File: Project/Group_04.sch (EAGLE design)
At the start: 29 parts, among them J1 POWER_JACKPTH_LOCK, U1 +12v

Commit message: modified frame and fixed component
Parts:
- U$1: device mylibrary_1:TMUX1208 -> Group_04_Library:TMUX1208
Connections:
- new net N$2: U$1.EN
- net 5V: no longer U$1.EN
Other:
- note added: "4-Channel I2C"
- note added: "Analog Temperature Sensor"
- note added: "I2C Connectors"
- note added: "Light sensor"
- note added: "Power"
- note added: "The I2C expander is used to connect several BME280 sensors outside the PCB through these connectors"
- moved on the sheet: C1, C2, C3, D1, J1, J2, J3, J4, J5, J6, J7, J8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

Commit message: fixed error on 5V pin
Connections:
- removed net N$2: U$1.EN
- net 5V: now also U$1.EN
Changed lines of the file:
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@@
 <part name="GND5" library="SparkFun-PowerSymbols" deviceset="GND" device=""/>
 <part name="J4" library="SparkFun-Connectors" deviceset="CONN_08" device="LOCK"/>
-<part name="SUPPLY8" library="SparkFun-PowerSymbols" deviceset="5V" device=""/>
 <part name="GND6" library="SparkFun-PowerSymbols" deviceset="GND" device=""/>
 <part name="C3" library="SparkFun-Capacitors" deviceset="0.1UF" device="-KIT-EZ-50V-20%" value="0.1uF"/>
@@
 <part name="U$1" library="Group_04_Library" deviceset="TMUX1208" device=""/>
 <part name="FRAME2" library="frames" library_urn="urn:adsk.eagle:library:229" deviceset="A4L-LOC" device=""/>
+<part name="SUPPLY8" library="SparkFun-PowerSymbols" deviceset="5V" device=""/>
 </parts>
 <sheets>
@@
 <attribute name="NAME" x="370.84" y="112.268" size="1.778" layer="95" font="vector"/>
 </instance>
-<instance part="SUPPLY8" gate="G$1" x="429.26" y="88.9" smashed="yes" rot="R270">
-<attribute name="VALUE" x="432.054" y="88.9" size="1.778" layer="96" rot="R270" align="bottom-center"/>
-</instance>
 <instance part="GND6" gate="1" x="424.18" y="78.74" smashed="yes">
 <attribute name="VALUE" x="424.18" y="78.486" size="1.778" layer="96" align="top-center"/>
@@
 <attribute name="LAST_DATE_TIME" x="494.03" y="20.32" size="2.286" layer="94"/>
 <attribute name="SHEET" x="507.365" y="15.24" size="2.54" layer="94"/>
+</instance>
+<instance part="SUPPLY8" gate="G$1" x="449.58" y="88.9" smashed="yes">
+<attribute name="VALUE" x="449.58" y="91.694" size="1.778" layer="96" align="bottom-center"/>
 </instance>
 </instances>
@@
 <junction x="429.26" y="119.38"/>
 </segment>
+<segment>
+<pinref part="U$1" gate="G$1" pin="EN"/>
+<pinref part="SUPPLY8" gate="G$1" pin="5V"/>
+<wire x1="421.64" y1="88.9" x2="449.58" y2="88.9" width="0.1524" layer="91"/>
+</segment>
 </net>
 <net name="MUX_OUT/1.4C" class="0">
@@
 </segment>
 </net>
-<net name="N$2" class="0">
-<segment>
-<pinref part="SUPPLY8" gate="G$1" pin="5V"/>
-<wire x1="421.64" y1="88.9" x2="429.26" y2="88.9" width="0.1524" layer="91"/>
-<pinref part="U$1" gate="G$1" pin="EN"/>
-</segment>
-</net>

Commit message: fixed mux connections
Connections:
- removed net MUX_A0/1.3C: U$1.A0
- removed net MUX_A0/2.3C: U$3.P_1.7
- removed net MUX_A1/1.4C: U$1.A1
- removed net MUX_A1/2.3C: U$3.P_1.6
- removed net MUX_A2/1.4C: U$1.A2
- removed net MUX_A2/2.3C: U$3.P_1.5
- removed net MUX_OUT/1.4C: U$1.D
- removed net MUX_OUT/2.5C: U$3.P_1.4
- new net MUX_A0: U$1.A0, U$3.P_1.7
- new net MUX_A1: U$1.A1, U$3.P_1.6
- new net MUX_A2: U$1.A2, U$3.P_1.5
- new net MUX_OUT: U$1.D, U$3.P_1.4
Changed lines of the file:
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@@
-</segment>
-</net>
-<net name="MUX_OUT/1.4C" class="0">
-<segment>
-<wire x1="421.64" y1="93.98" x2="424.18" y2="93.98" width="0.1524" layer="91"/>
-<label x="424.18" y="93.98" size="1.778" layer="95" xref="yes"/>
-<pinref part="U$1" gate="G$1" pin="D"/>
 </segment>
 </net>
@@
 </segment>
 </net>
-<net name="MUX_A0/1.3C" class="0">
+<net name="MUX_OUT" class="0">
 <segment>
-<wire x1="421.64" y1="109.22" x2="424.18" y2="109.22" width="0.1524" layer="91"/>
-<label x="424.18" y="109.22" size="1.778" layer="95" xref="yes"/>
-<pinref part="U$1" gate="G$1" pin="A0"/>
+<pinref part="U$3" gate="G$1" pin="P_1.4"/>
+<wire x1="127" y1="99.06" x2="127" y2="101.6" width="0.1524" layer="91"/>
+<label x="127" y="101.6" size="1.778" layer="95" rot="R90" xref="yes"/>
+</segment>
+<segment>
+<wire x1="421.64" y1="93.98" x2="424.18" y2="93.98" width="0.1524" layer="91"/>
+<label x="424.18" y="93.98" size="1.778" layer="95" xref="yes"/>
+<pinref part="U$1" gate="G$1" pin="D"/>
 </segment>
 </net>
-<net name="MUX_A1/1.4C" class="0">
+<net name="MUX_A2" class="0">
+<segment>
+<pinref part="U$3" gate="G$1" pin="P_1.5"/>
+<wire x1="124.46" y1="99.06" x2="124.46" y2="101.6" width="0.1524" layer="91"/>
+<label x="124.46" y="101.6" size="1.778" layer="95" rot="R90" xref="yes"/>
+</segment>
+<segment>
+<wire x1="421.64" y1="99.06" x2="424.18" y2="99.06" width="0.1524" layer="91"/>
+<label x="424.18" y="99.06" size="1.778" layer="95" xref="yes"/>
+<pinref part="U$1" gate="G$1" pin="A2"/>
+</segment>
+</net>
+<net name="MUX_A1" class="0">
+<segment>
+<pinref part="U$3" gate="G$1" pin="P_1.6"/>
+<wire x1="121.92" y1="99.06" x2="121.92" y2="101.6" width="0.1524" layer="91"/>
+<label x="121.92" y="101.6" size="1.778" layer="95" rot="R90" xref="yes"/>
+</segment>
 <segment>
 <wire x1="421.64" y1="104.14" x2="424.18" y2="104.14" width="0.1524" layer="91"/>
@@
 </segment>
 </net>
-<net name="MUX_A2/1.4C" class="0">
-<segment>
-<wire x1="421.64" y1="99.06" x2="424.18" y2="99.06" width="0.1524" layer="91"/>
-<label x="424.18" y="99.06" size="1.778" layer="95" xref="yes"/>
-<pinref part="U$1" gate="G$1" pin="A2"/>
-</segment>
-</net>
-<net name="MUX_OUT/2.5C" class="0">
-<segment>
-<pinref part="U$3" gate="G$1" pin="P_1.4"/>
-<wire x1="127" y1="99.06" x2="127" y2="101.6" width="0.1524" layer="91"/>
-<label x="127" y="101.6" size="1.778" layer="95" rot="R90" xref="yes"/>
-</segment>
-</net>
-<net name="MUX_A2/2.3C" class="0">
-<segment>
-<pinref part="U$3" gate="G$1" pin="P_1.5"/>
-<wire x1="124.46" y1="99.06" x2="124.46" y2="101.6" width="0.1524" layer="91"/>
-<label x="124.46" y="101.6" size="1.778" layer="95" rot="R90" xref="yes"/>
-</segment>
-</net>
-<net name="MUX_A1/2.3C" class="0">
-<segment>
-<pinref part="U$3" gate="G$1" pin="P_1.6"/>
-<wire x1="121.92" y1="99.06" x2="121.92" y2="101.6" width="0.1524" layer="91"/>
-<label x="121.92" y="101.6" size="1.778" layer="95" rot="R90" xref="yes"/>
-</segment>
-</net>
-<net name="MUX_A0/2.3C" class="0">
+<net name="MUX_A0" class="0">
 <segment>
 <pinref part="U$3" gate="G$1" pin="P_1.7"/>
@@
 <label x="119.38" y="101.6" size="1.778" layer="95" rot="R90" xref="yes"/>
 </segment>
+<segment>
+<wire x1="421.64" y1="109.22" x2="424.18" y2="109.22" width="0.1524" layer="91"/>
+<pinref part="U$1" gate="G$1" pin="A0"/>
+<label x="424.18" y="109.22" size="1.778" layer="95" xref="yes"/>
+</segment>
 </net>

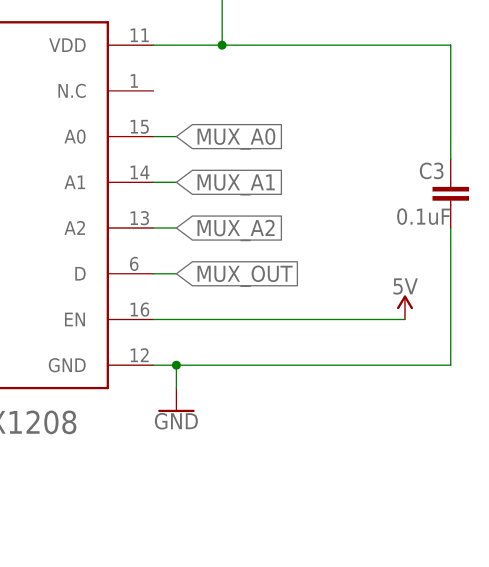
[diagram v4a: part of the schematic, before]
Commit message: fixed mux component schematic
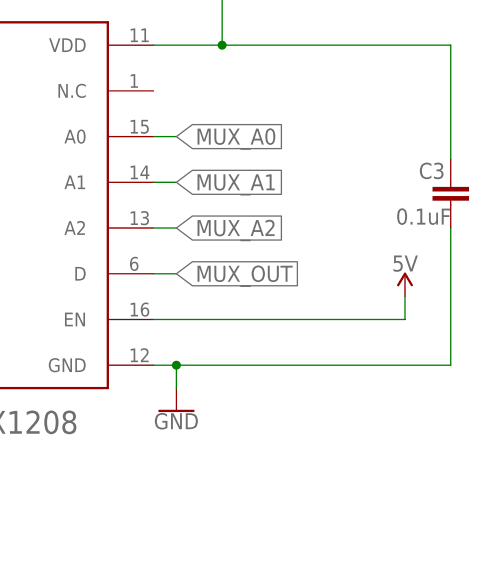
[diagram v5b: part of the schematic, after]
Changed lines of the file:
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@@
 <part name="J8" library="SparkFun-Connectors" deviceset="CONN_02" device=""/>
 <part name="FRAME1" library="frames" library_urn="urn:adsk.eagle:library:229" deviceset="A4L-LOC" device=""/>
+<part name="FRAME2" library="frames" library_urn="urn:adsk.eagle:library:229" deviceset="A4L-LOC" device=""/>
 <part name="U$1" library="Group_04_Library" deviceset="TMUX1208" device=""/>
-<part name="FRAME2" library="frames" library_urn="urn:adsk.eagle:library:229" deviceset="A4L-LOC" device=""/>
 <part name="SUPPLY8" library="SparkFun-PowerSymbols" deviceset="5V" device=""/>
 </parts>
@@
 <attribute name="SHEET" x="238.125" y="15.24" size="2.54" layer="94"/>
 </instance>
-<instance part="U$1" gate="G$1" x="406.4" y="106.68" smashed="yes">
-<attribute name="NAME" x="396.24" y="124.46" size="2.54" layer="95"/>
-<attribute name="VALUE" x="396.24" y="76.2" size="2.54" layer="96"/>
-</instance>
 <instance part="FRAME2" gate="G$1" x="276.86" y="10.16" smashed="yes">
 <attribute name="DRAWING_NAME" x="494.03" y="25.4" size="2.54" layer="94"/>
@@
 <attribute name="SHEET" x="507.365" y="15.24" size="2.54" layer="94"/>
 </instance>
-<instance part="SUPPLY8" gate="G$1" x="449.58" y="88.9" smashed="yes">
-<attribute name="VALUE" x="449.58" y="91.694" size="1.778" layer="96" align="bottom-center"/>
+<instance part="U$1" gate="G$1" x="406.4" y="106.68" smashed="yes">
+<attribute name="NAME" x="396.24" y="124.46" size="2.54" layer="95"/>
+<attribute name="VALUE" x="396.24" y="76.2" size="2.54" layer="96"/>
+</instance>
+<instance part="SUPPLY8" gate="G$1" x="449.58" y="91.44" smashed="yes">
+<attribute name="VALUE" x="449.58" y="94.234" size="1.778" layer="96" align="bottom-center"/>
 </instance>
 </instances>
@@
 </segment>
 <segment>
-<pinref part="C3" gate="G$1" pin="2"/>
+<pinref part="U$1" gate="G$1" pin="GND"/>
 <wire x1="421.64" y1="83.82" x2="424.18" y2="83.82" width="0.1524" layer="91"/>
-<wire x1="424.18" y1="83.82" x2="454.66" y2="83.82" width="0.1524" layer="91"/>
-<wire x1="454.66" y1="83.82" x2="454.66" y2="99.06" width="0.1524" layer="91"/>
 <pinref part="GND6" gate="1" pin="GND"/>
 <wire x1="424.18" y1="81.28" x2="424.18" y2="83.82" width="0.1524" layer="91"/>
+<pinref part="C3" gate="G$1" pin="2"/>
+<wire x1="454.66" y1="83.82" x2="454.66" y2="99.06" width="0.1524" layer="91"/>
+<wire x1="424.18" y1="83.82" x2="454.66" y2="83.82" width="0.1524" layer="91"/>
 <junction x="424.18" y="83.82"/>
-<pinref part="U$1" gate="G$1" pin="GND"/>
 </segment>
 <segment>
@@
 <segment>
 <pinref part="U$1" gate="G$1" pin="EN"/>
+<wire x1="421.64" y1="88.9" x2="449.58" y2="88.9" width="0.1524" layer="91"/>
 <pinref part="SUPPLY8" gate="G$1" pin="5V"/>
-<wire x1="421.64" y1="88.9" x2="449.58" y2="88.9" width="0.1524" layer="91"/>
+<wire x1="449.58" y1="91.44" x2="449.58" y2="88.9" width="0.1524" layer="91"/>
 </segment>
 </net>
@@
 <wire x1="381" y1="106.68" x2="383.54" y2="106.68" width="0.1524" layer="91"/>
 <wire x1="383.54" y1="106.68" x2="383.54" y2="114.3" width="0.1524" layer="91"/>
+<pinref part="U$1" gate="G$1" pin="S2"/>
 <wire x1="383.54" y1="114.3" x2="391.16" y2="114.3" width="0.1524" layer="91"/>
-<pinref part="U$1" gate="G$1" pin="S2"/>
 </segment>
 </net>
@@
 <wire x1="381" y1="104.14" x2="386.08" y2="104.14" width="0.1524" layer="91"/>
 <wire x1="386.08" y1="104.14" x2="386.08" y2="109.22" width="0.1524" layer="91"/>
+<pinref part="U$1" gate="G$1" pin="S3"/>
 <wire x1="386.08" y1="109.22" x2="391.16" y2="109.22" width="0.1524" layer="91"/>
-<pinref part="U$1" gate="G$1" pin="S3"/>
 </segment>
 </net>
@@
 <wire x1="381" y1="101.6" x2="388.62" y2="101.6" width="0.1524" layer="91"/>
 <wire x1="388.62" y1="101.6" x2="388.62" y2="104.14" width="0.1524" layer="91"/>
+<pinref part="U$1" gate="G$1" pin="S4"/>
 <wire x1="388.62" y1="104.14" x2="391.16" y2="104.14" width="0.1524" layer="91"/>
-<pinref part="U$1" gate="G$1" pin="S4"/>
-</segment>
-</net>
-<net name="N$14" class="0">
-<segment>
-<pinref part="J4" gate="G$1" pin="4"/>
-<wire x1="381" y1="99.06" x2="391.16" y2="99.06" width="0.1524" layer="91"/>
-<pinref part="U$1" gate="G$1" pin="S5"/>
 </segment>
 </net>
@@
 <pinref part="J4" gate="G$1" pin="3"/>
 <wire x1="381" y1="96.52" x2="388.62" y2="96.52" width="0.1524" layer="91"/>
+<pinref part="U$1" gate="G$1" pin="S6"/>
+<wire x1="388.62" y1="93.98" x2="391.16" y2="93.98" width="0.1524" layer="91"/>
 <wire x1="388.62" y1="96.52" x2="388.62" y2="93.98" width="0.1524" layer="91"/>
-<wire x1="388.62" y1="93.98" x2="391.16" y2="93.98" width="0.1524" layer="91"/>
-<pinref part="U$1" gate="G$1" pin="S6"/>
 </segment>
 </net>
@@
 <wire x1="381" y1="93.98" x2="386.08" y2="93.98" width="0.1524" layer="91"/>
 <wire x1="386.08" y1="93.98" x2="386.08" y2="88.9" width="0.1524" layer="91"/>
+<pinref part="U$1" gate="G$1" pin="S7"/>
 <wire x1="386.08" y1="88.9" x2="391.16" y2="88.9" width="0.1524" layer="91"/>
-<pinref part="U$1" gate="G$1" pin="S7"/>
 </segment>
 </net>
@@
 <pinref part="J4" gate="G$1" pin="1"/>
 <wire x1="381" y1="91.44" x2="381" y2="83.82" width="0.1524" layer="91"/>
+<pinref part="U$1" gate="G$1" pin="S8"/>
 <wire x1="381" y1="83.82" x2="391.16" y2="83.82" width="0.1524" layer="91"/>
-<pinref part="U$1" gate="G$1" pin="S8"/>
 </segment>
 </net>
@@
 </segment>
 <segment>
+<pinref part="U$1" gate="G$1" pin="D"/>
 <wire x1="421.64" y1="93.98" x2="424.18" y2="93.98" width="0.1524" layer="91"/>
 <label x="424.18" y="93.98" size="1.778" layer="95" xref="yes"/>
-<pinref part="U$1" gate="G$1" pin="D"/>
 </segment>
 </net>
@@
 </segment>
 <segment>
+<pinref part="U$1" gate="G$1" pin="A2"/>
 <wire x1="421.64" y1="99.06" x2="424.18" y2="99.06" width="0.1524" layer="91"/>
 <label x="424.18" y="99.06" size="1.778" layer="95" xref="yes"/>
-<pinref part="U$1" gate="G$1" pin="A2"/>
 </segment>
 </net>
@@
 </segment>
 <segment>
+<pinref part="U$1" gate="G$1" pin="A1"/>
 <wire x1="421.64" y1="104.14" x2="424.18" y2="104.14" width="0.1524" layer="91"/>
 <label x="424.18" y="104.14" size="1.778" layer="95" xref="yes"/>
-<pinref part="U$1" gate="G$1" pin="A1"/>
 </segment>
 </net>
@@
 </segment>
 <segment>
+<pinref part="U$1" gate="G$1" pin="A0"/>
 <wire x1="421.64" y1="109.22" x2="424.18" y2="109.22" width="0.1524" layer="91"/>
-<pinref part="U$1" gate="G$1" pin="A0"/>
 <label x="424.18" y="109.22" size="1.778" layer="95" xref="yes"/>
 </segment>
@@
 </segment>
 </net>
+<net name="N$5" class="0">
+<segment>
+<pinref part="J4" gate="G$1" pin="4"/>
+<pinref part="U$1" gate="G$1" pin="S5"/>
+<wire x1="381" y1="99.06" x2="391.16" y2="99.06" width="0.1524" layer="91"/>
+</segment>
+</net>
